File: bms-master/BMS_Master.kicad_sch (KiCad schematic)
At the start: 79 parts, among them J1 Conn_PWR, J2 Conn_CAN, J3 Conn_CSR, J4 PROG, J5 Conn_CSROUT, J6 BMS_M_IN, J7 Conn_Fault, SW1 SW_SPST, U1 AP2204K-ADJ, U2 AP2204K-ADJ, U3 SN65HVD256D, U4 STM32F103C8Tx, U5 TLV2371DBV, U6 TLV2371DBV, U7 BQ79600-Q1, Y1 8M, Y2 32.768k

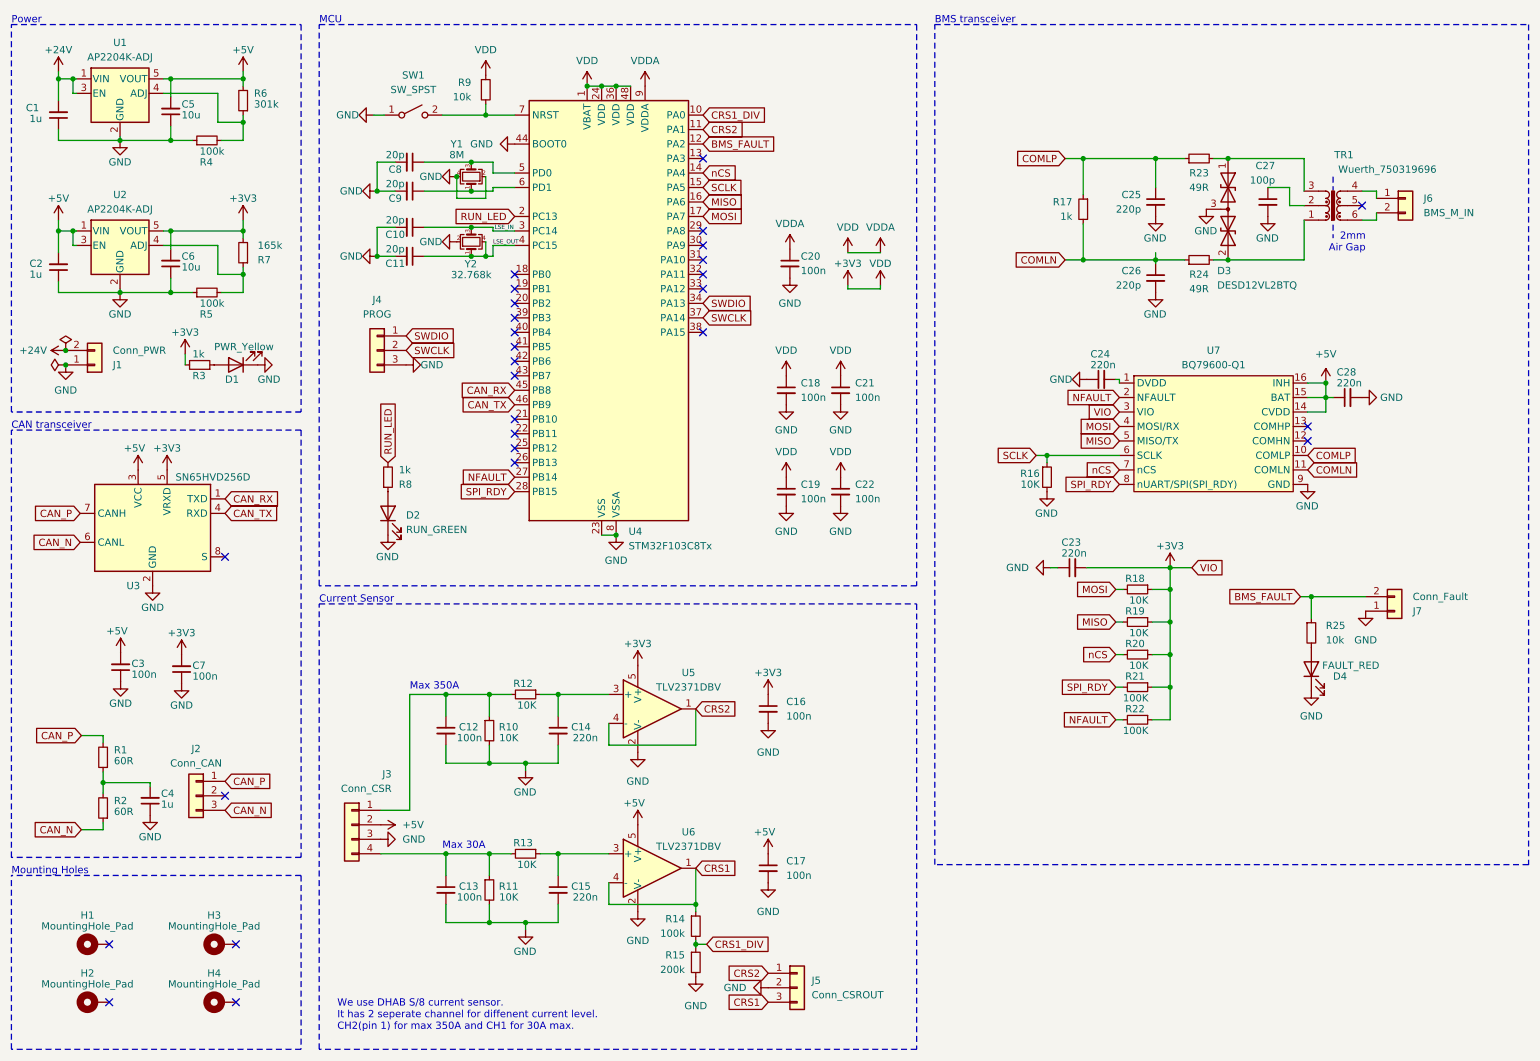
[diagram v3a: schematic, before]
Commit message: Add sd card to BMS master and change commu to UART
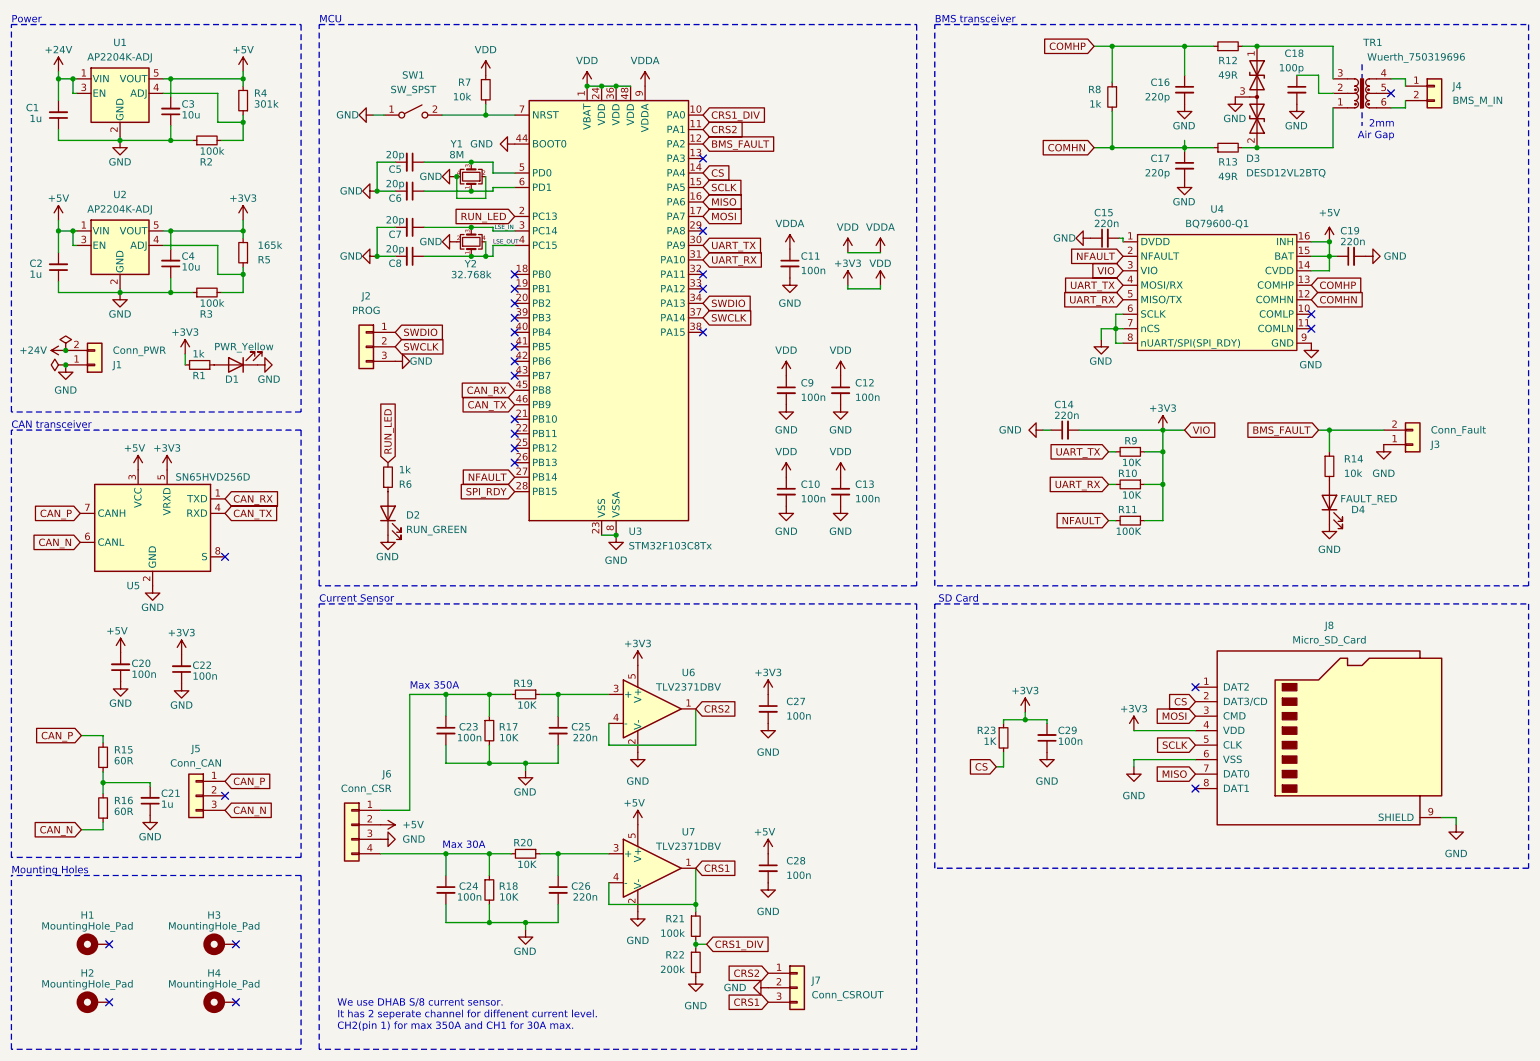
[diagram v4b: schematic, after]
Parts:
- removed R16, R20: 10K, Resistor_SMD:R_0603_1608Metric, symbol Device:R_Small
- removed R21: 100K, Resistor_SMD:R_0603_1608Metric, symbol Device:R_Small
- added C29: 100n, Capacitor_SMD:C_0603_1608Metric, symbol Device:C_Small
- added J8: Micro_SD_Card, symbol Connector:Micro_SD_Card
- added R23: 1K, Resistor_SMD:R_0603_1608Metric, symbol Device:R_Small
- renumbered C19 to C10, C20 to C11, C21 to C12, C22 to C13, C23 to C14, C24 to C15, C25 to C16, C26 to C17, C27 to C18, C28 to C19, C3 to C20, C4 to C21, C7 to C22, C12 to C23, C13 to C24, C14 to C25, C15 to C26, C16 to C27, C17 to C28, C5 to C3, C6 to C4, C8 to C5, C9 to C6, C10 to C7, C11 to C8, C18 to C9, J4 to J2, J7 to J3, J6 to J4, J2 to J5, J3 to J6, J5 to J7, R3 to R1, R19 to R10, R22 to R11, R23 to R12, R24 to R13, R25 to R14, R1 to R15, R2 to R16, R10 to R17, R11 to R18, R12 to R19, R4 to R2, R13 to R20, R14 to R21, R15 to R22, R5 to R3, R6 to R4, R7 to R5, R8 to R6, R9 to R7, R17 to R8, R18 to R9, U4 to U3, U7 to U4, U3 to U5, U5 to U6, U6 to U7
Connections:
- net +3V3: now also C29.2, J8.4 (VDD), R23.1
- net GND: now also U4.6 (SCLK), U4.7 (nCS), U4.8 (nUART/SPI(SPI_RDY)), C29.1, J8.6 (VSS), J8.9 (SHIELD)
- net MISO: now also J8.7 (DAT0); no longer R10.2, U4.5 (MISO/TX)
- net MOSI: now also J8.3 (CMD); no longer R9.2, U4.4 (MOSI/RX)
- net SCLK: now also J8.5 (CLK); no longer U4.6 (SCLK)
- net SPI_RDY: no longer U4.8 (nUART/SPI(SPI_RDY))
- net COMHN: now reaches U4.12 (COMHN)
- net COMHN: now also C17.1, R13.1, R8.2
- net COMHP: now reaches U4.13 (COMHP)
- net COMHP: now also C16.1, R12.1, R8.1
- net UART_TX: now reaches U3.30 (PA9)
- net UART_TX: now also R9.2, U4.4 (MOSI/RX)
- net UART_RX: now reaches U3.31 (PA10)
- net UART_RX: now also R10.2, U4.5 (MISO/TX)
- removed net COMLN: C17.1, R13.1, R8.2, U4.11 (COMLN)
- removed net COMLP: C16.1, R12.1, R8.1, U4.10 (COMLP)
- net nCS renamed CS
- net CS: now also J8.2 (DAT3/CD), R23.2; no longer U4.7 (nCS)
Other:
- note added: "SD Card"
- moved on the sheet: C14, C15, C16, C17, C18, C19, D3, D4, J2, J3, J4, R10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

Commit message: Link sd card slot to footprint
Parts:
- J8: footprint (none) -> Connector_Card:microSD_HC_Molex_47219-2001
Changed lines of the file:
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@@
       (effects (font (size 1.27 1.27)))
     )
-    (property "Footprint" "" (at 274.955 131.445 0)
+    (property "Footprint" "Connector_Card:microSD_HC_Molex_47219-2001" (at 274.955 131.445 0)
       (effects (font (size 1.27 1.27)) hide)
     )

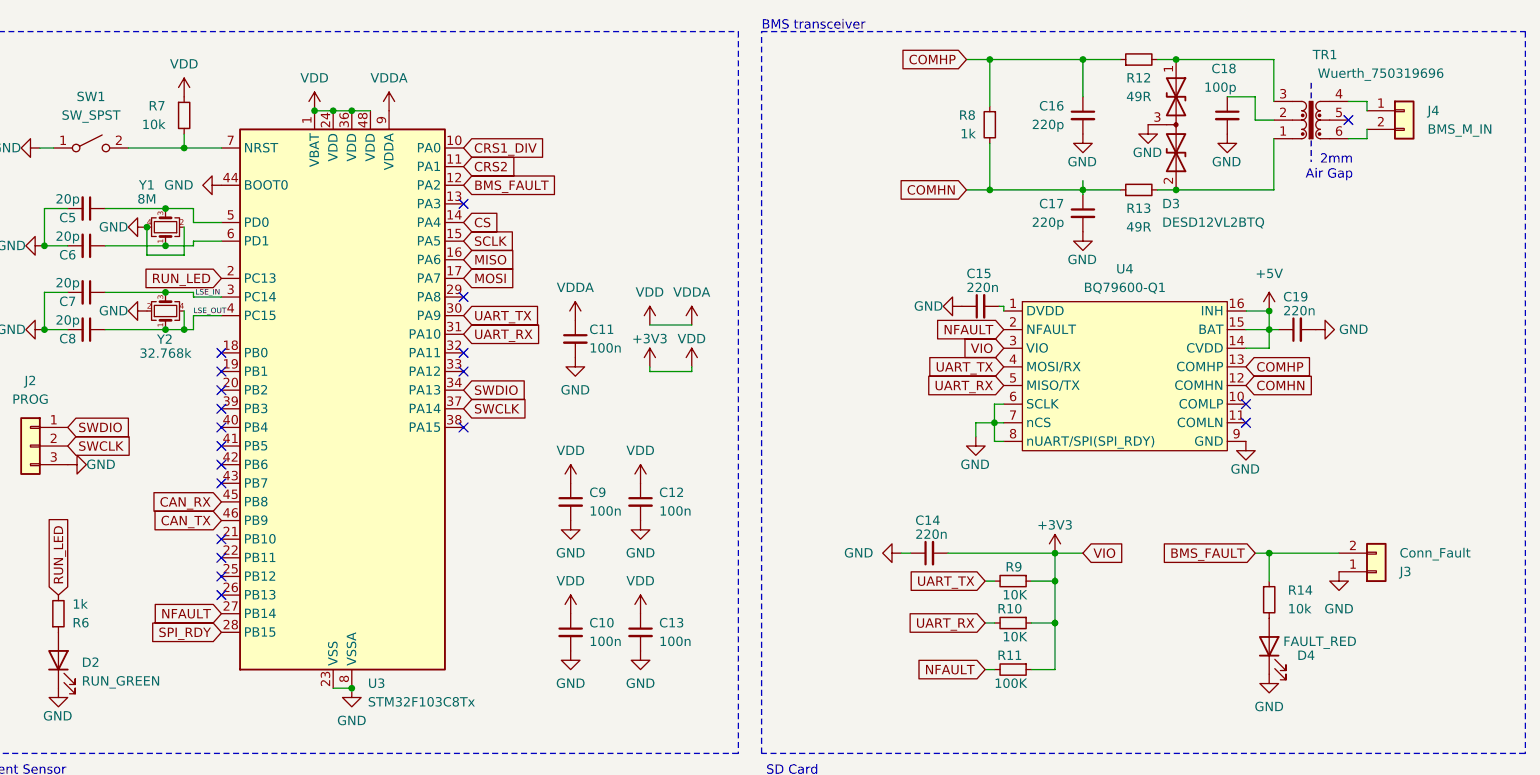
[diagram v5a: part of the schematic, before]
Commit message: Redo BMS master layout again, SD card slot added
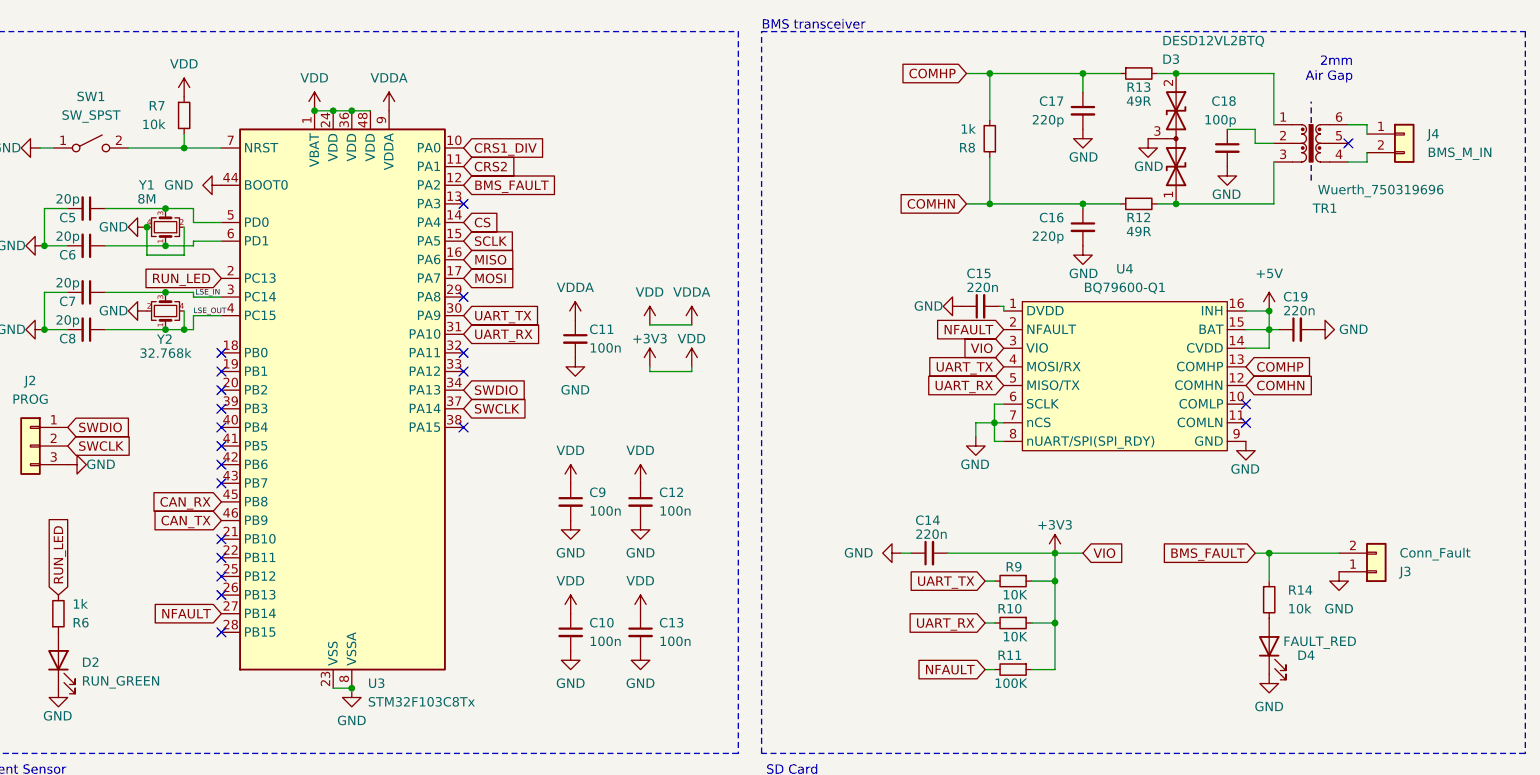
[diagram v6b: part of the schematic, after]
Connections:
- net COMHN: now also C16.1, R12.1, R8.1; no longer C17.1, R13.1, R8.2
- net COMHP: now also C17.1, R13.1, R8.2; no longer C16.1, R12.1, R8.1
- net at TR1.4: now also J4.2 (Pin_2); no longer J4.1 (Pin_1)
- net at TR1.6: now also J4.1 (Pin_1); no longer J4.2 (Pin_2)
- net SPI_RDY: no longer names the net of U3.28 (PB15)
- no-connect marks 28 -> 29
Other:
- moved on the sheet: C16, C17, C18, D3, J4, R12, R13, R8, TR1

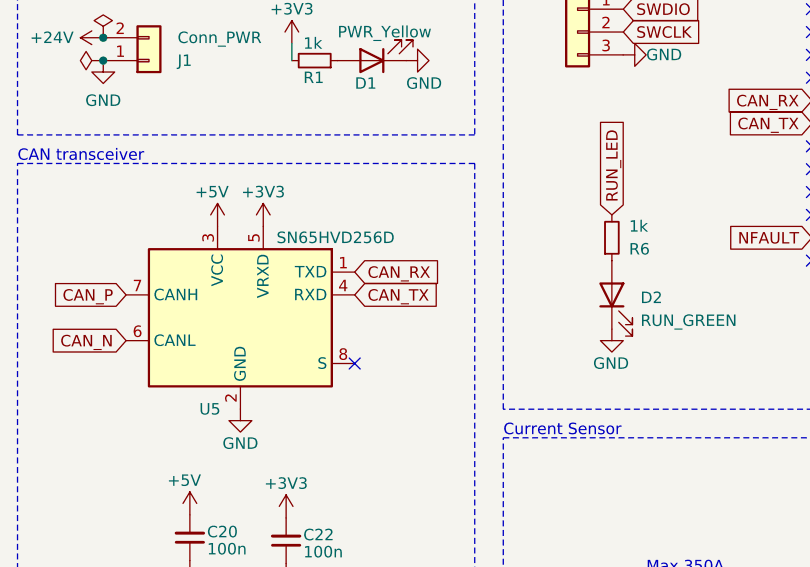
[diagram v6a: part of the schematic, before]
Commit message: Fix bms master can bus tx/rx opposite issue
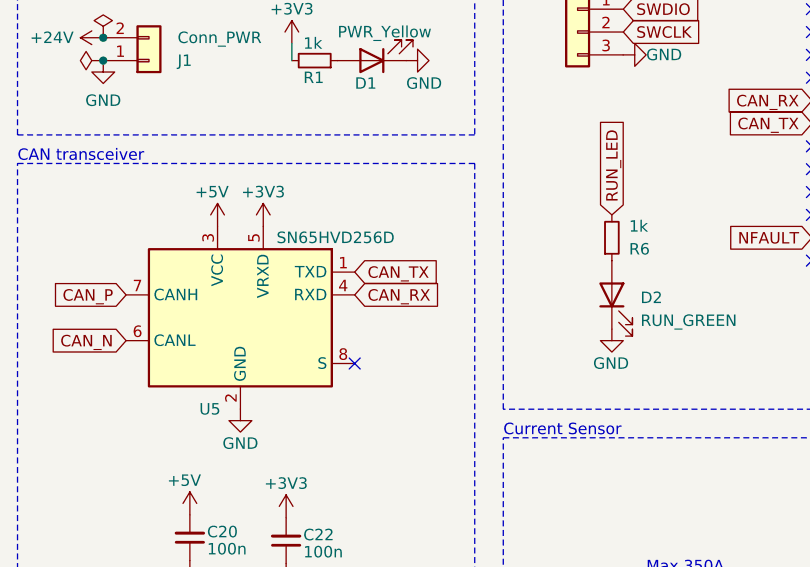
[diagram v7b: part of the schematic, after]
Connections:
- net CAN_RX: now also U5.4 (RXD); no longer U5.1 (TXD)
- net CAN_TX: now also U5.1 (TXD); no longer U5.4 (RXD)
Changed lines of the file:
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@@
     )
   )
-  (global_label "CAN_RX" (shape input) (at 52.705 98.425 0) (fields_autoplaced)
+  (global_label "CAN_RX" (shape input) (at 52.705 100.965 0) (fields_autoplaced)
     (effects (font (size 1.27 1.27)) (justify left))
-    (property "Intersheetrefs" "${INTERSHEET_REFS}" (at 62.8264 98.425 0)
+    (property "Intersheetrefs" "${INTERSHEET_REFS}" (at 62.8264 100.965 0)
       (effects (font (size 1.27 1.27)) (justify left) hide)
     )
@@
     )
   )
-  (global_label "CAN_TX" (shape input) (at 52.705 100.965 0) (fields_autoplaced)
+  (global_label "CAN_TX" (shape input) (at 52.705 98.425 0) (fields_autoplaced)
     (effects (font (size 1.27 1.27)) (justify left))
-    (property "Intersheetrefs" "${INTERSHEET_REFS}" (at 62.524 100.965 0)
+    (property "Intersheetrefs" "${INTERSHEET_REFS}" (at 62.524 98.425 0)
       (effects (font (size 1.27 1.27)) (justify left) hide)
     )
